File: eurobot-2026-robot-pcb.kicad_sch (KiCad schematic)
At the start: 1 part, among them U1 ESP32-S3-DevKitC

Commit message: restart sch
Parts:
- removed U1: ESP32-S3-DevKitC, PCM_Espressif:ESP32-S3-DevKitC, symbol PCM_Espressif:ESP32-S3-DevKitC
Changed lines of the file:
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@@
 		(company "Game Team SLSC")
-	)
-	(symbol
-		(lib_id "PCM_Espressif:ESP32-S3-DevKitC")
-		(at 66.04 74.93 0)
-		(unit 1)
-		(exclude_from_sim no)
-		(in_bom yes)
-		(on_board yes)
-		(dnp no)
-		(fields_autoplaced yes)
-		(property "Reference" "U1"
-			(at 68.1833 120.65 0)
-			(effects
-				(font
-					(size 1.27 1.27)
-				)
-				(justify left)
-			)
-		)
-		(property "Value" "ESP32-S3-DevKitC"
-			(at 68.1833 123.19 0)
-			(effects
-				(font
-					(size 1.27 1.27)
-				)
-				(justify left)
-			)
-		)
-		(property "Footprint" "PCM_Espressif:ESP32-S3-DevKitC"
-			(at 66.04 132.08 0)
-			(effects
-				(font
-					(size 1.27 1.27)
-				)
-				(hide yes)
-			)
-		)
-		(property "Datasheet" ""
-			(at 6.35 77.47 0)
-			(effects
-				(font
-					(size 1.27 1.27)
-				)
-				(hide yes)
-			)
-		)
-		(property "Description" "ESP32-S3-DevKitC"
-			(at 66.04 74.93 0)
-			(effects
-				(font
-					(size 1.27 1.27)
-				)
-				(hide yes)
-			)
-		)
-		(pin "39"
-		)
-		(pin "43"
-		)
-		(pin "23"
-		)
-		(pin "19"
-		)
-		(pin "38"
-		)
-		(pin "14"
-		)
-		(pin "36"
-		)
-		(pin "8"
-		)
-		(pin "18"
-		)
-		(pin "5"
-		)
-		(pin "4"
-		)
-		(pin "12"
-		)
-		(pin "31"
-		)
-		(pin "9"
-		)
-		(pin "16"
-		)
-		(pin "22"
-		)
-		(pin "7"
-		)
-		(pin "41"
-		)
-		(pin "3"
-		)
-		(pin "24"
-		)
-		(pin "26"
-		)
-		(pin "44"
-		)
-		(pin "42"
-		)
-		(pin "40"
-		)
-		(pin "37"
-		)
-		(pin "2"
-		)
-		(pin "21"
-		)
-		(pin "1"
-		)
-		(pin "25"
-		)
-		(pin "13"
-		)
-		(pin "6"
-		)
-		(pin "15"
-		)
-		(pin "17"
-		)
-		(pin "28"
-		)
-		(pin "20"
-		)
-		(pin "32"
-		)
-		(pin "35"
-		)
-		(pin "10"
-		)
-		(pin "29"
-		)
-		(pin "11"
-		)
-		(pin "34"
-		)
-		(pin "30"
-		)
-		(pin "27"
-		)
-		(pin "33"
-		)
-		(instances
-			(project ""
-				(path "/b7a41ac4-1d1a-4287-8cea-fdfe5ab5ee00"
-					(reference "U1")
-					(unit 1)
-				)
-			)
-		)
 	)
 	(sheet_instances

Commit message: First stuff
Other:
- added sheet Arms (Servos.kicad_sch)
- added sheet Logic (logic.kicad_sch)
- added sheet Power (alim.kicad_sch)
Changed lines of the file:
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@@
 	(generator "eeschema")
 	(generator_version "9.0")
-	(paper "A3")
+	(paper "A5")
 	(title_block
 		(title "Eurobot 2026 robot PCB")
@@
 		(company "Game Team SLSC")
 	)
+	(sheet
+		(at 93.98 19.05)
+		(size 15.24 7.62)
+		(exclude_from_sim no)
+		(in_bom yes)
+		(on_board yes)
+		(dnp no)
+		(fields_autoplaced yes)
+		(stroke
+			(width 0.1524)
+			(type solid)
+		)
+		(fill
+			(color 0 0 0 0.0000)
+		)
+		(property "Sheetname" "Arms"
+			(at 93.98 18.3384 0)
+			(effects
+				(font
+					(size 1.27 1.27)
+				)
+				(justify left bottom)
+			)
+		)
+		(property "Sheetfile" "Servos.kicad_sch"
+			(at 93.98 27.2546 0)
+			(effects
+				(font
+					(size 1.27 1.27)
+				)
+				(justify left top)
+			)
+		)
+		(instances
+			(project "eurobot-2026-robot-pcb"
+				(path "/b7a41ac4-1d1a-4287-8cea-fdfe5ab5ee00"
+					(page "4")
+				)
+			)
+		)
+	)
+	(sheet
+		(at 13.97 15.24)
+		(size 13.97 3.81)
+		(exclude_from_sim no)
+		(in_bom yes)
+		(on_board yes)
+		(dnp no)
+		(fields_autoplaced yes)
+		(stroke
+			(width 0.1524)
+			(type solid)
+		)
+		(fill
+			(color 0 0 0 0.0000)
+		)
+		(property "Sheetname" "Power"
+			(at 13.97 14.5284 0)
+			(effects
+				(font
+					(size 1.27 1.27)
+				)
+				(justify left bottom)
+			)
+		)
+		(property "Sheetfile" "alim.kicad_sch"
+			(at 13.97 19.6346 0)
+			(effects
+				(font
+					(size 1.27 1.27)
+				)
+				(justify left top)
+			)
+		)
+		(instances
+			(project "eurobot-2026-robot-pcb"
+				(path "/b7a41ac4-1d1a-4287-8cea-fdfe5ab5ee00"
+					(page "2")
+				)
+			)
+		)
+	)
+	(sheet
+		(at 50.8 20.32)
+		(size 16.51 3.81)
+		(exclude_from_sim no)
+		(in_bom yes)
+		(on_board yes)
+		(dnp no)
+		(fields_autoplaced yes)
+		(stroke
+			(width 0.1524)
+			(type solid)
+		)
+		(fill
+			(color 0 0 0 0.0000)
+		)
+		(property "Sheetname" "Logic"
+			(at 50.8 19.6084 0)
+			(effects
+				(font
+					(size 1.27 1.27)
+				)
+				(justify left bottom)
+			)
+		)
+		(property "Sheetfile" "logic.kicad_sch"
+			(at 50.8 24.7146 0)
+			(effects
+				(font
+					(size 1.27 1.27)
+				)
+				(justify left top)
+			)
+		)
+		(instances
+			(project "eurobot-2026-robot-pcb"
+				(path "/b7a41ac4-1d1a-4287-8cea-fdfe5ab5ee00"
+					(page "3")
+				)
+			)
+		)
+	)
 	(sheet_instances

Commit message: Add most off the stuff
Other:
- removed sheet Arms
- sheet Logic: file logic.kicad_sch -> Servos.kicad_sch
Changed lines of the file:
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@@
 			(color 0 0 0 0.0000)
 		)
-		(property "Sheetname" "Arms"
+		(property "Sheetname" "Logic"
 			(at 93.98 18.3384 0)
 			(effects
@@
 				)
 			)
-		)
-	)
-	(sheet
-		(at 50.8 20.32)
-		(size 16.51 3.81)
-		(exclude_from_sim no)
-		(in_bom yes)
-		(on_board yes)
-		(dnp no)
-		(fields_autoplaced yes)
-		(stroke
-			(width 0.1524)
-			(type solid)
-		)
-		(fill
-			(color 0 0 0 0.0000)
-		)
-		(property "Sheetname" "Logic"
-			(at 50.8 19.6084 0)
-			(effects
-				(font
-					(size 1.27 1.27)
-				)
-				(justify left bottom)
-			)
-		)
-		(property "Sheetfile" "logic.kicad_sch"
-			(at 50.8 24.7146 0)
-			(effects
-				(font
-					(size 1.27 1.27)
-				)
-				(justify left top)
-			)
-		)
-		(instances
-			(project "eurobot-2026-robot-pcb"
-				(path "/b7a41ac4-1d1a-4287-8cea-fdfe5ab5ee00"
-					(page "3")
-				)
-			)

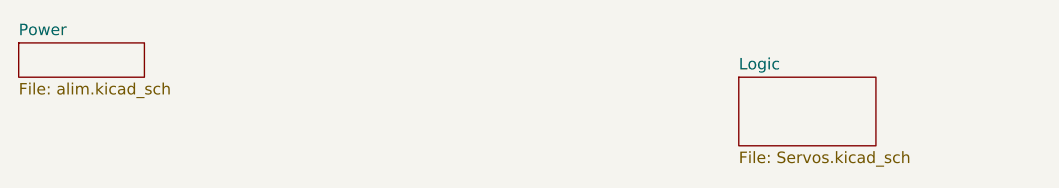
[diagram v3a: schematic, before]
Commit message: Add relay for BAU + fixes
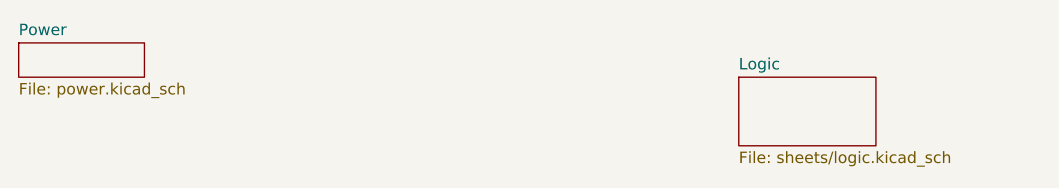
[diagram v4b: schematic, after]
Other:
- sheet Logic: file Servos.kicad_sch -> sheets/logic.kicad_sch
- sheet Power: file alim.kicad_sch -> power.kicad_sch
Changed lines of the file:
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@@
 			)
 		)
-		(property "Sheetfile" "Servos.kicad_sch"
+		(property "Sheetfile" "sheets/logic.kicad_sch"
 			(at 93.98 27.2546 0)
 			(effects
@@
 			)
 		)
-		(property "Sheetfile" "alim.kicad_sch"
+		(property "Sheetfile" "power.kicad_sch"
 			(at 13.97 19.6346 0)
 			(effects
